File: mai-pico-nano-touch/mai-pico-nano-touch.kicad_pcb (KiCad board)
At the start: 2 copper layers, 99 x 24 mm, 7 parts, among them J1 Conn_01x04, J2 Conn_01x34, U1 MPR121-Module, U2 MPR121-Module, U3 MPR121-Module

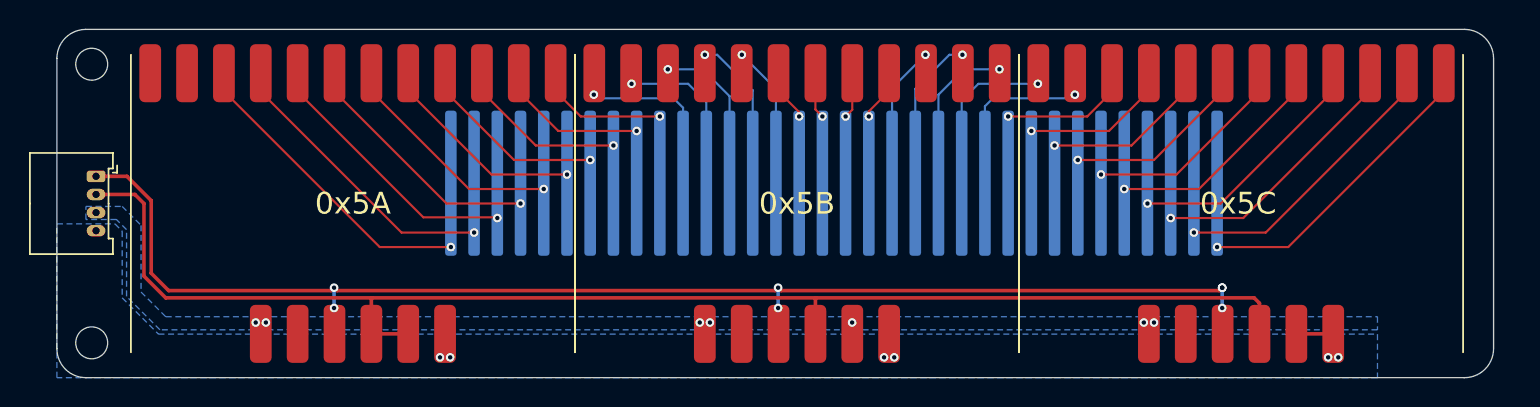
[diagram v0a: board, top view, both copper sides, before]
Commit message: Add screwholes to touch board
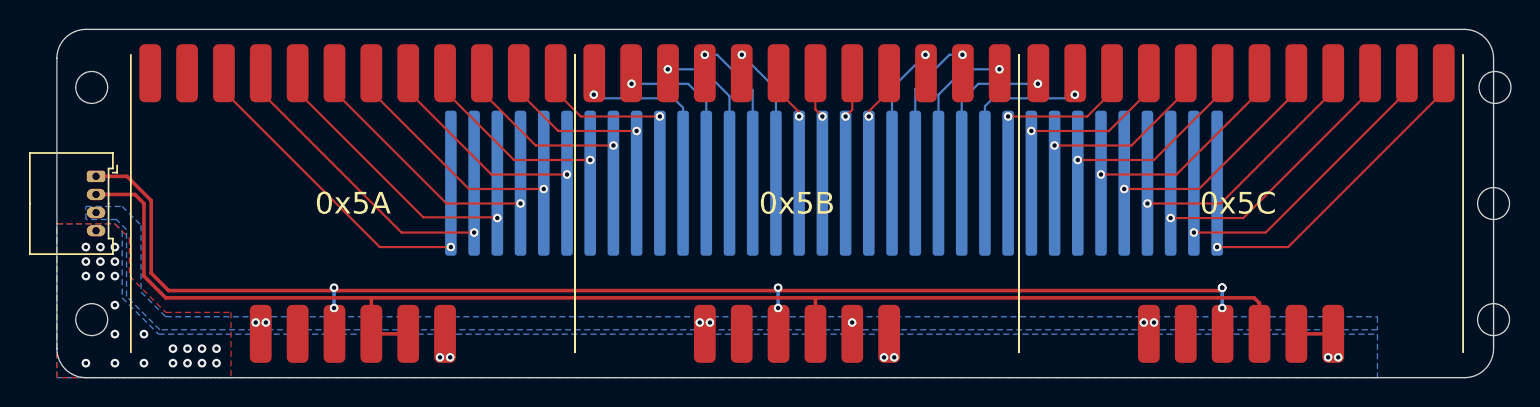
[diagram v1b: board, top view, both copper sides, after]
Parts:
- added REF**: MountingHole_2.2mm_M2, MountingHole:MountingHole_2.2mm_M2, F.Cu at (148.1, 76.0)
- added REF**: MountingHole_2.2mm_M2, MountingHole:MountingHole_2.2mm_M2, F.Cu at (148.0, 92.0)
- added REF**: MountingHole_2.2mm_M2, MountingHole:MountingHole_2.2mm_M2, F.Cu at (148.0, 84.0)
- moved REF** 1.60 mm to (51.4, 92.0)
- moved REF** 1.60 mm to (51.4, 76.0)
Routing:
- net GND: vias 6 -> 29
- added copper zone on F.Cu, net GND

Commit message: Update touch board silkscreen
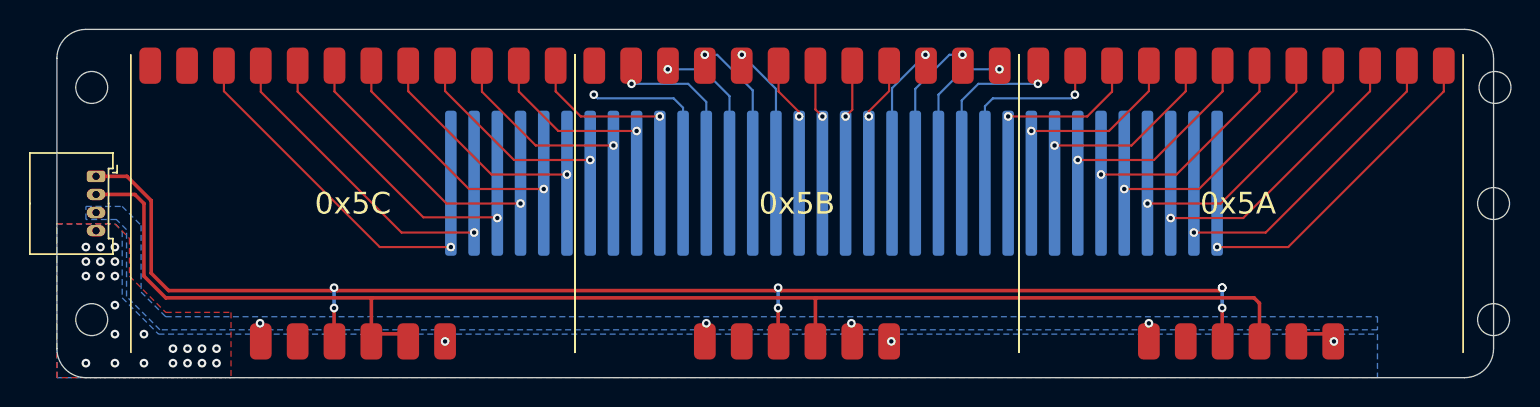
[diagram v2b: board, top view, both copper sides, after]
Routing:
- net /SCL: track 88.4 -> 95.3 mm
- net /E11: track 11.8 -> 13.8 mm
- net /E21: track 12.0 -> 10.7 mm
- net /E22: track 12.3 -> 11.0 mm
- net /E19: track 4.82 -> 3.57 mm
- net /E15: track 11.0 -> 9.80 mm
- net /E20: track 11.3 -> 10.1 mm
- net /E18: track 4.39 -> 3.70 mm
- net VDD: vias 7 -> 4
- net GND: vias 29 -> 26

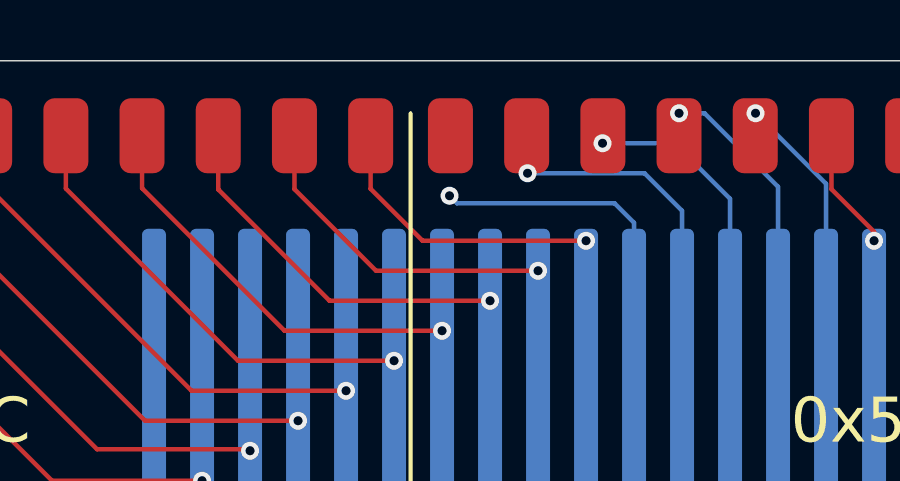
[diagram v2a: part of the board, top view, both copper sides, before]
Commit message: Fix PCB not connected
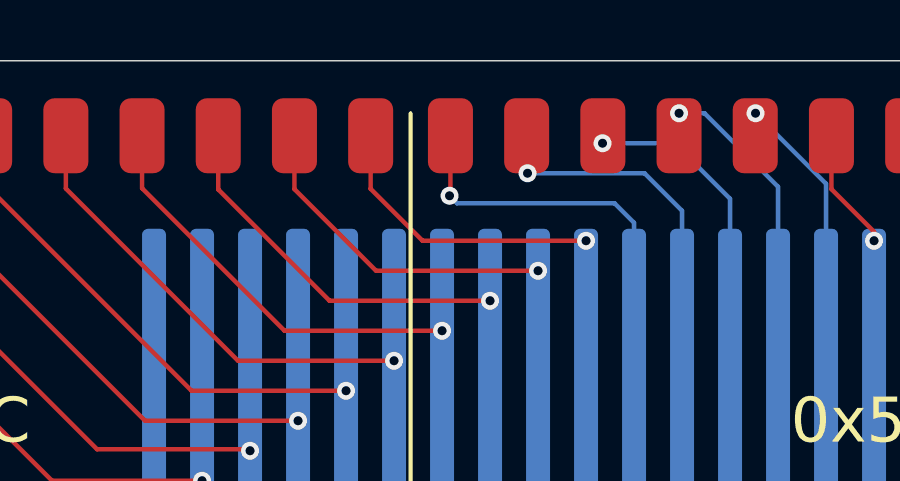
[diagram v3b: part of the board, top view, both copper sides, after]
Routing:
- net /E24: track 11.7 -> 13.7 mm
